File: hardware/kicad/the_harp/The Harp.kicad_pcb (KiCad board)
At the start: 4 copper layers, 56 x 94.5 mm, 41 parts, among them J401 PJ-063AH, J402 NRJ6HM-1, J403 NRJ6HM-1, J404 NRJ6HM-1, J405 Footswitch, J406 NRJ6HM-1, K401 EE2-5NU, Q401 2N7002, Q402 2N7002, SW101 SPDT, SW102 SPDT, SW103 SPDT, U401 NCP718ASN500T1G, U402 NCP718ASN330T1G

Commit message: Draw the first schematic: Timekeeper circuits on the Relic grid
Seven sheets generated by scripts/harp_schematic from a circuit spec and
net-traced against it (195 parts, 48 global nets, no shorts or single-pin
nets): Controls and LEDs, MCU (STM32H750VBT6 LQFP-100, W25Q128 on QUADSPI
bank 2), Power (TPS54202 + NCP718, as the Timekeeper), Jacks and Bypass
(four jacks, Relic relay bypass, LED drivers, footswitches, expression
buffer), Codec (AK4621EF, OPA2348 VCOM buffers), ADC Driver (THS4522) and
Analog In and Out (OPA1656 buffer, OPA1688 difference amplifiers).

Replaces the Relic Power and IO sheet; removes its regulator footprints
from the board and detaches the remaining footprints for relinking by
reference. Docs: shared Alchemist/Relic/Harp face standard and the toggle
conflict it exposes, pin map, differences from the Timekeeper.

Co-Authored-By: Claude Opus 5.5 <noreply@anthropic.com>
Claude-Session: https://claude.ai/code/session_01ToUUHuo6mg178NkLtQkDLg
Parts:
- removed C401: 47u, Capacitor_SMD:C_Elec_6.3x5.8
- removed C402: 100n, Capacitor_SMD:C_0603_1608Metric
- removed C403, C404, C405, C406: 2u2, Capacitor_SMD:C_0603_1608Metric
- removed C407: 10u, Capacitor_SMD:CP_Elec_4x5.4
- removed D401: SS34, Diode_SMD:D_SMA
- removed R401: 47R, Resistor_SMD:R_0805_2012Metric
- removed R402, R403: 4k7, Resistor_SMD:R_0805_2012Metric
- removed U401: NCP718ASN500T1G, Package_TO_SOT_SMD:TSOT-23-5
- removed U402: NCP718ASN330T1G, Package_TO_SOT_SMD:TSOT-23-5
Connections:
- C408 pad 1: FSW_IN -> (no net)
- C408 pad 2: GND -> (no net)
- D402 pad 1: /Power and IO/RELAY_COIL -> (no net)
- D402 pad 2: /Power and IO/RELAY_LOW -> (no net)
- J401 pad 1: GND -> (no net)
- J401 pad 2: /Power and IO/DC_IN -> (no net)
- J402 pad R: unconnected-(J402-PadR) -> (no net)
- J402 pad RN: unconnected-(J402-PadRN) -> (no net)
- J402 pad S: GND -> (no net)
- J402 pad SN: unconnected-(J402-PadSN) -> (no net)
- J402 pad T: /Power and IO/IN -> (no net)
- J402 pad TN: unconnected-(J402-PadTN) -> (no net)
- J403 pad R: unconnected-(J403-PadR) -> (no net)
- J403 pad RN: unconnected-(J403-PadRN) -> (no net)
- J403 pad S: GND -> (no net)
- J403 pad SN: unconnected-(J403-PadSN) -> (no net)
- J403 pad T: /Power and IO/OUT -> (no net)
- J403 pad TN: unconnected-(J403-PadTN) -> (no net)
- J405 pad 1: /Power and IO/FSW -> (no net)
- J405 pad 2: GND -> (no net)
- K401 pad 1: /Power and IO/RELAY_COIL -> (no net)
- K401 pad 10: GND -> (no net)
- K401 pad 12: /Power and IO/RELAY_LOW -> (no net)
- K401 pad 3: /Power and IO/IN -> (no net)
- K401 pad 4: /Power and IO/OUT -> (no net)
- K401 pad 5: EFFECT_OUT -> (no net)
- K401 pad 8: /Power and IO/IN -> (no net)
- K401 pad 9: EFFECT_IN -> (no net)
- Q401 pad 1: /Power and IO/RELAY_G -> (no net)
- Q401 pad 2: GND -> (no net)
- Q401 pad 3: /Power and IO/RELAY_LOW -> (no net)
- Q402 pad 1: /Power and IO/LED_G -> (no net)
- Q402 pad 2: GND -> (no net)
- Q402 pad 3: /Power and IO/FSW_LED -> (no net)
- R404 pad 1: /Power and IO/FSW_LED_K -> (no net)
- R404 pad 2: /Power and IO/FSW_LED -> (no net)
- R405 pad 1: +9V -> (no net)
- R405 pad 2: /Power and IO/RELAY_COIL -> (no net)
- R406 pad 1: RELAY_DRV -> (no net)
- R406 pad 2: /Power and IO/RELAY_G -> (no net)
- R407 pad 1: /Power and IO/RELAY_G -> (no net)
- R407 pad 2: GND -> (no net)
- R408 pad 1: LED_DRV -> (no net)
- R408 pad 2: /Power and IO/LED_G -> (no net)
- R409 pad 1: /Power and IO/LED_G -> (no net)
- R409 pad 2: GND -> (no net)
- R410 pad 1: /Power and IO/FSW -> (no net)
- R410 pad 2: FSW_IN -> (no net)

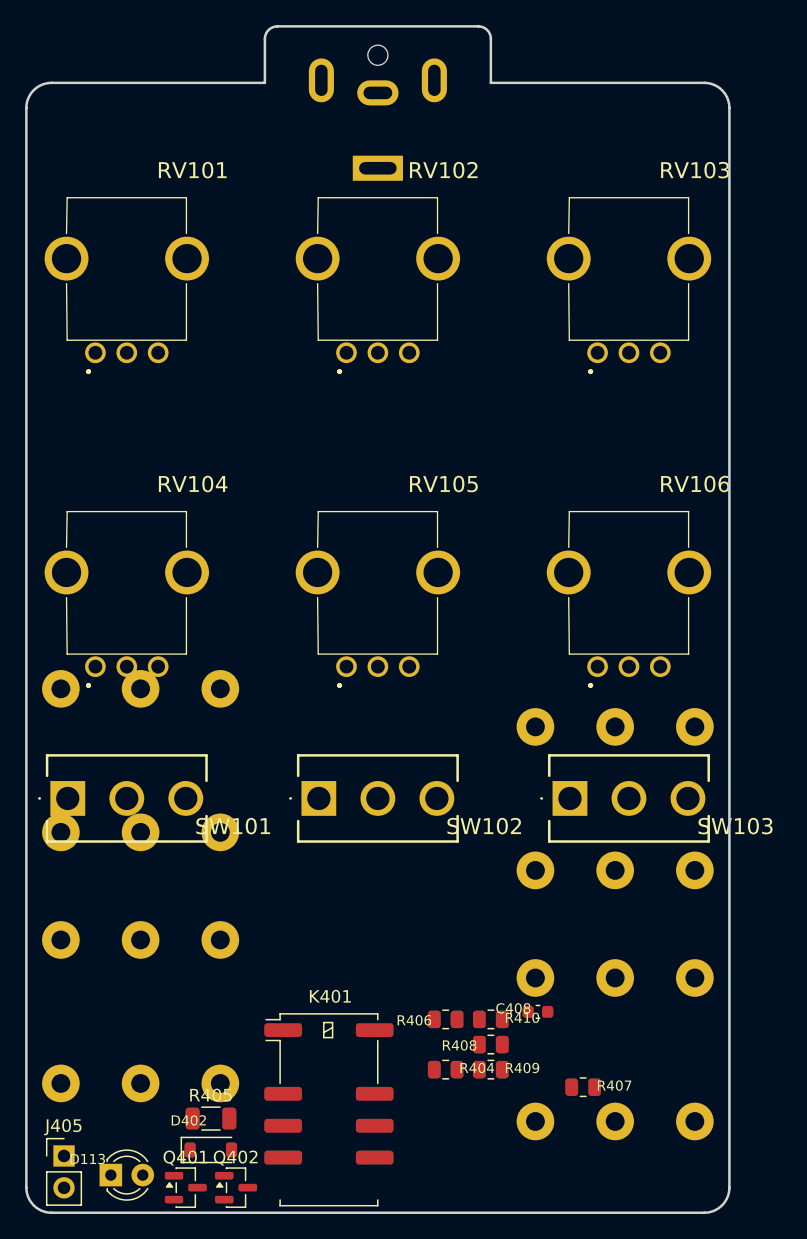
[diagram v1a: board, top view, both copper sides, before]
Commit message: Follow The Alchemist's shared parts: NMJ6HCD2 jacks, G6K-2F-Y relay, JLCPCB numbers
- Jacks: Neutrik NMJ6HCD2 (JLCPCB HOOYA PJ-609BA, C309277); IN jack ring to
  GND as The Alchemist. PCB footprints copied from The Alchemist at its
  positions (origins 0.75/0.885 mm moved, nose axes unchanged).
- Relay: Omron G6K-2F-Y DC5 (C2982926), Alchemist pinout; PCB footprint at
  its position.
- Design and JLCPCB part numbers on the pots, relay drivers, LED drivers,
  footswitch RC, DC jack and the 5 V LDO; panel LEDs Kingbright WP710A10ID,
  dnp; footswitches on R2816 hand-solder pads, dnp.
- Docs: design brief decision 12, toggle conflict re-checked for the new
  jack geometry, stale OPA1656 mentions in pcb-plan corrected.
- Toggles not changed: The Alchemist's Taiway 100-DP6 is ON-ON-ON.

Co-Authored-By: Claude Opus 5.5 <noreply@anthropic.com>
Claude-Session: https://claude.ai/code/session_01ToUUHuo6mg178NkLtQkDLg
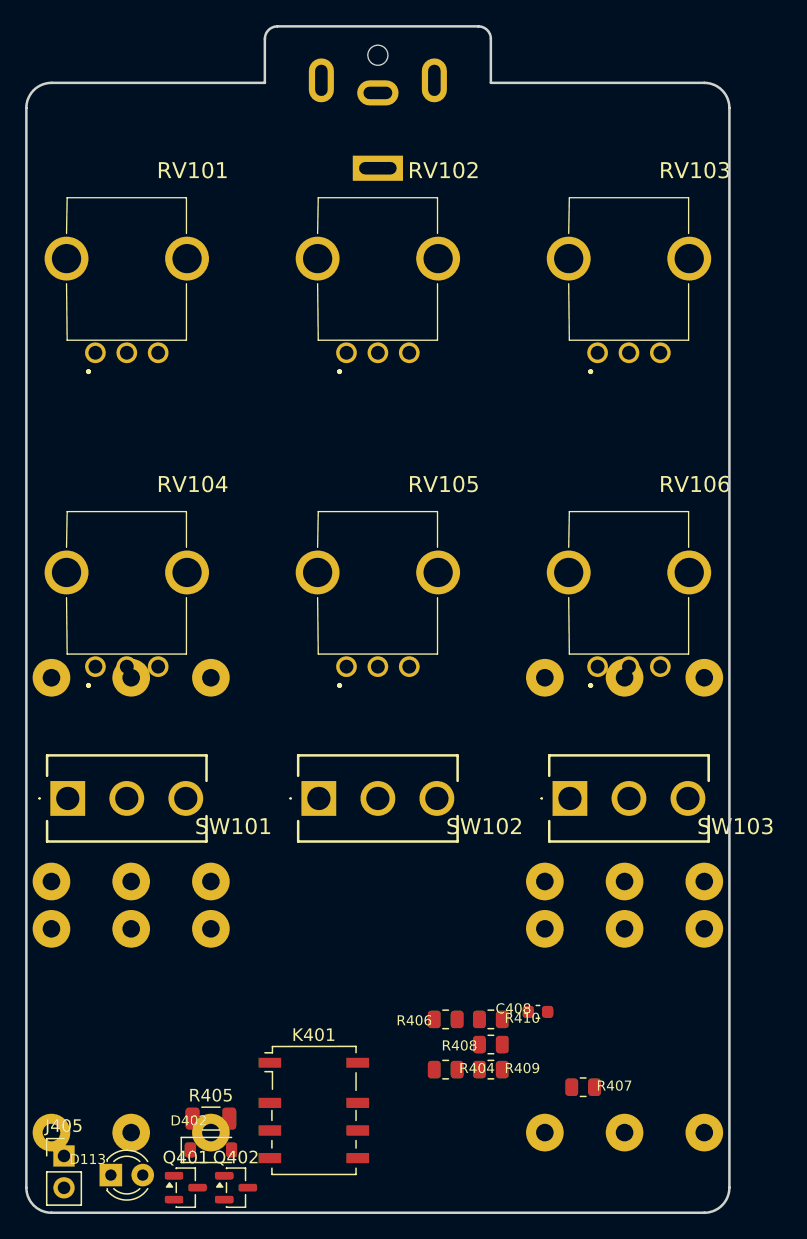
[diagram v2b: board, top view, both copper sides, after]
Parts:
- J402, J403, J404, J406: value NRJ6HM-1 -> NMJ6HCD2; footprint Connector_Audio:Jack_6.35mm_Neutrik_NRJ6HM-1_Horizontal -> Connector_Audio:Jack_6.35mm_Neutrik_NMJ6HCD2_Horizontal
- K401: value EE2-5NU -> G6K-2F-Y; footprint Relay_SMD:Relay_DPDT_Kemet_EE2_NU -> Relay_SMD:Relay_DPDT_Omron_G6K-2F-Y
- moved K401 1.20 mm to (143.4, 134.8)
- moved J402 1.16 mm to (161.8, 136.6)
- moved J403 1.16 mm to (135.2, 120.4)
- moved J404 1.16 mm to (135.2, 100.4)
- moved J406 1.16 mm to (161.8, 116.6)
